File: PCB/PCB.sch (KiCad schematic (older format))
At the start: 26 parts, among them J1 , J2 , J3 PROG, SW1 ADDR, U1 ATtiny806-M

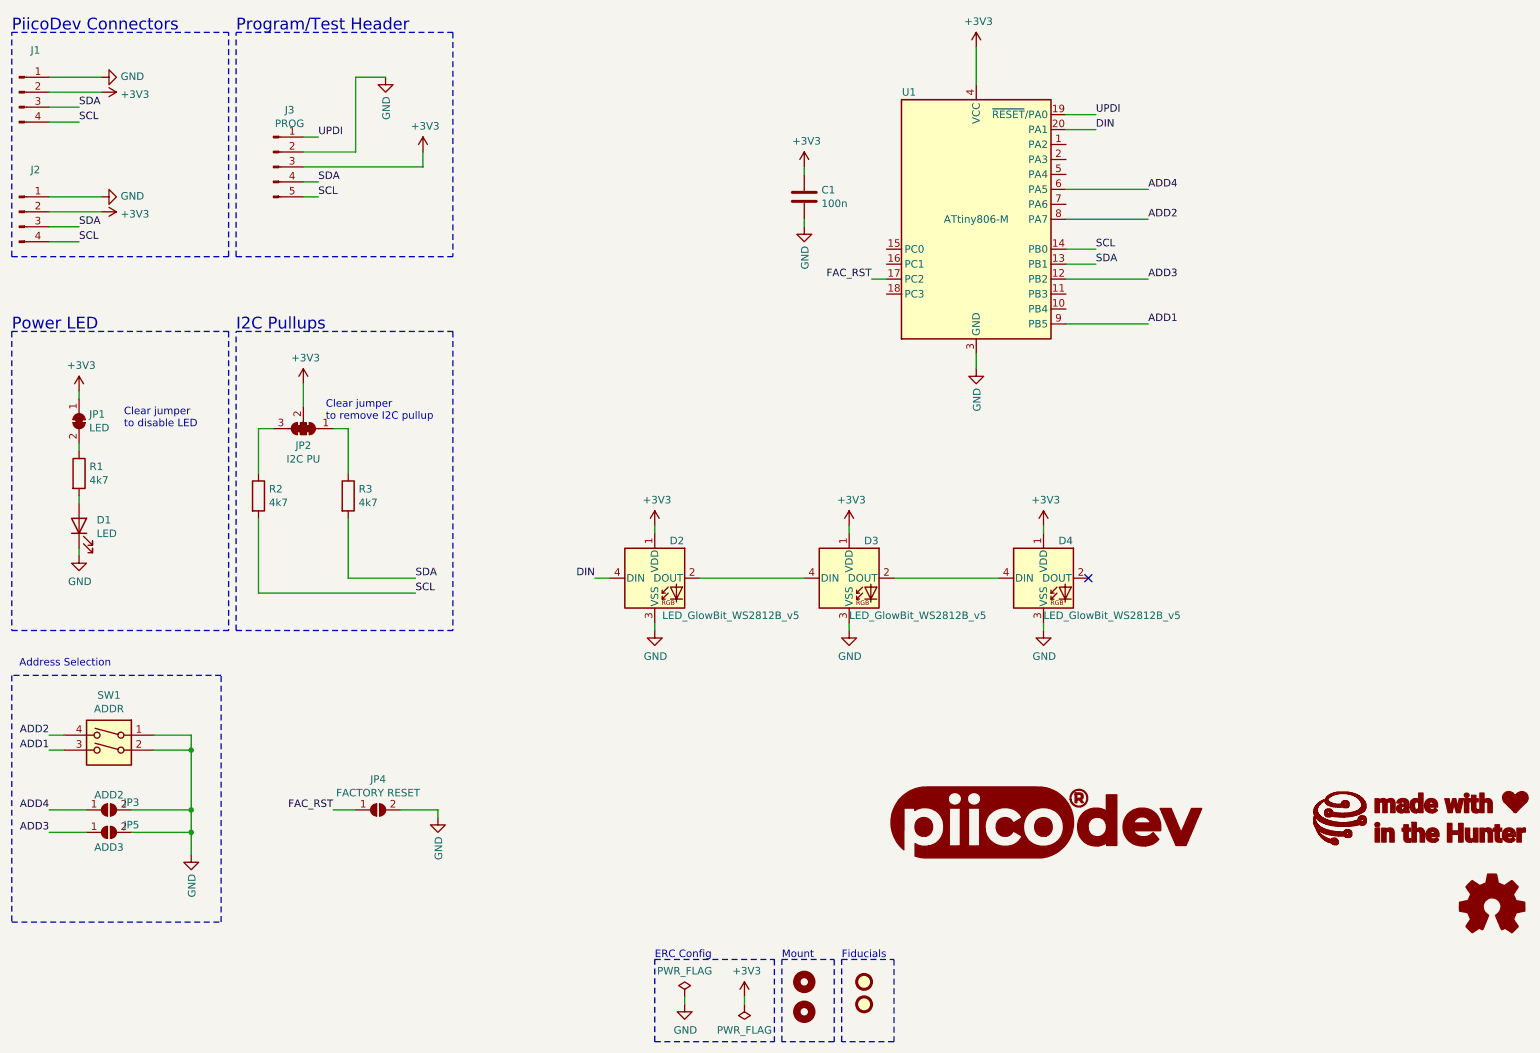
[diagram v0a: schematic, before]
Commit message: Make pwr LED user controllable
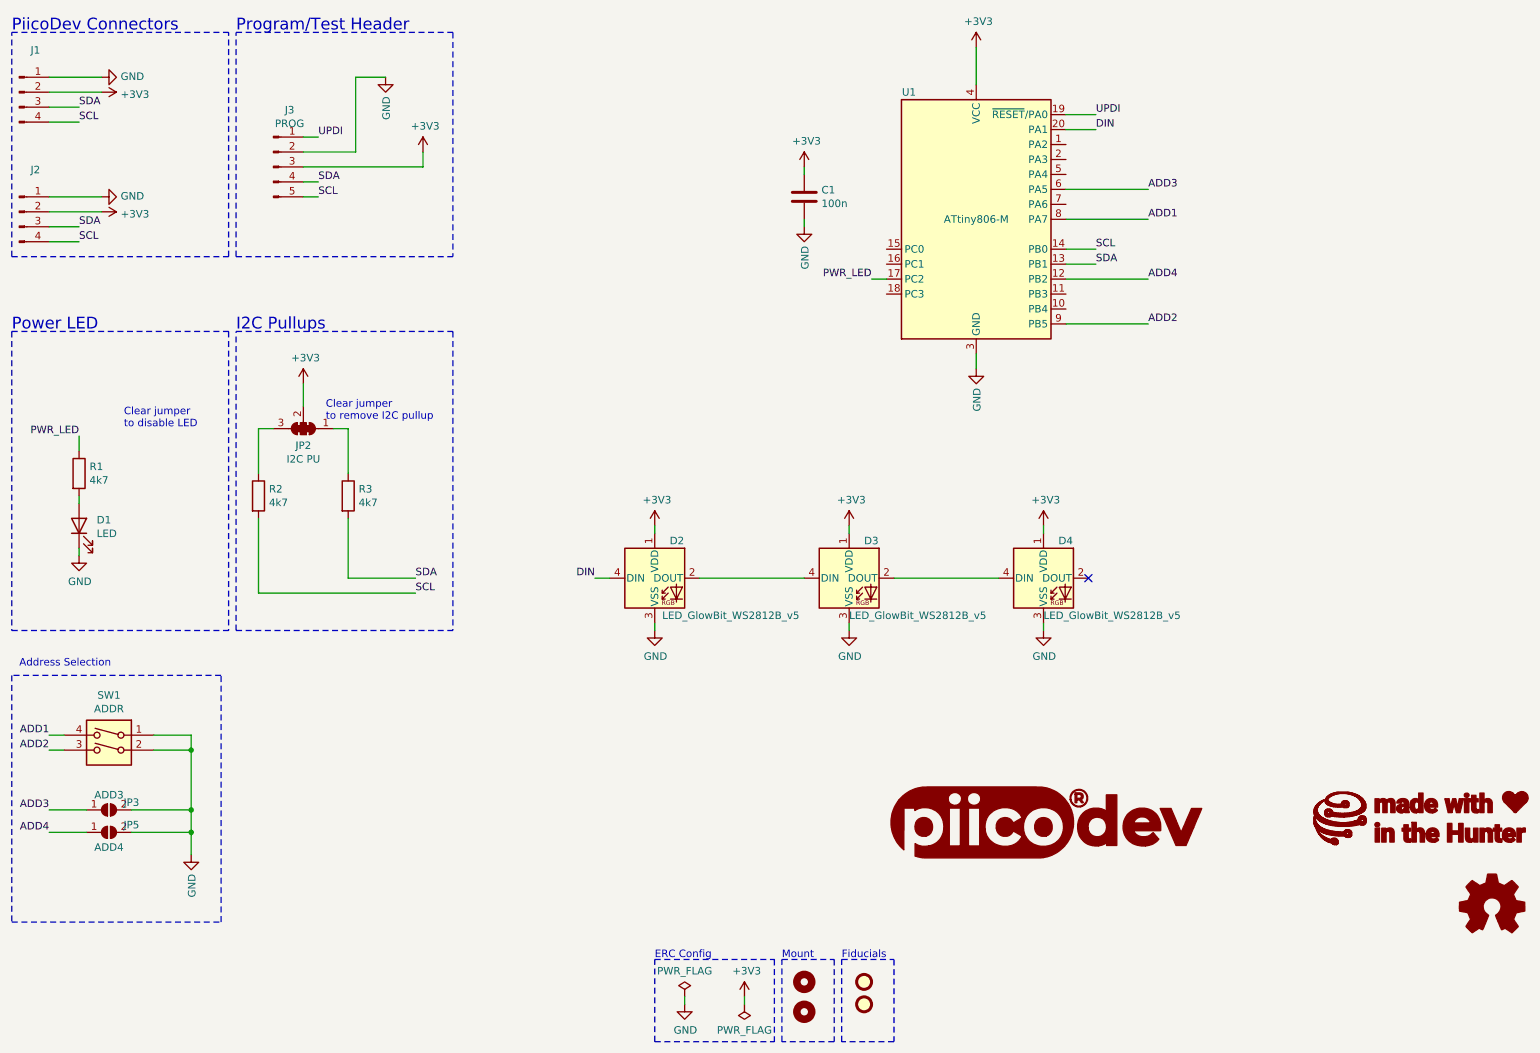
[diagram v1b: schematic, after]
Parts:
- removed JP1: LED, CoreElectronics_Components:SolderJumper-2_P1.3mm_Bridged_RoundedPad1.0x1.5mm, symbol Jumper:SolderJumper_2_Bridged
- removed JP4: FACTORY RESET, Jumper:SolderJumper-2_P1.3mm_Open_RoundedPad1.0x1.5mm, symbol Jumper:SolderJumper_2_Open
- J3: footprint CoreElectronics_Components:PiicoDev_ProgrammingHeader_2x03_P1.27mm_Vertical -> CoreElectronics_Components:PiicoDev_header_programming_test_1x05_P1.27mm_Vertical
- JP3: value ADD2 -> ADD3
- JP5: value ADD3 -> ADD4
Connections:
- net FAC_RST is gone; now on net PWR_LED: U1.17 (PC2)
- net ADD1: now also SW1.4, U1.8 (PA7); no longer SW1.3, U1.9 (PB5)
- net ADD2: now also SW1.3, U1.9 (PB5); no longer SW1.4, U1.8 (PA7)
- net ADD3: now also JP3.1 (A), U1.6 (PA5); no longer JP5.1 (A), U1.12 (PB2)
- net ADD4: now also JP5.1 (A), U1.12 (PB2); no longer JP3.1 (A), U1.6 (PA5)
- net PWR_LED: now reaches R1.1
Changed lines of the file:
@@
 Wire Wire Line
 	1450 4150 1450 4100
-Wire Wire Line
-	1450 3800 1450 3750
 $Comp
 L Device:R R1
@@
 F 3 "~" H 1450 3950 50  0001 C CNN
 	1    1450 3950
-	1    0    0    -1
-$EndComp
-Wire Wire Line
-	1450 3450 1450 3400
-$Comp
-L Jumper:SolderJumper_2_Bridged JP1
-U 1 1 60A1F615
-P 1450 3600
-F 0 "JP1" V 1404 3668 50  0000 L CNN
-F 1 "LED" V 1495 3668 50  0000 L CNN
-F 2 "CoreElectronics_Components:SolderJumper-2_P1.3mm_Bridged_RoundedPad1.0x1.5mm" H 1450 3600 50  0001 C CNN
-F 3 "~" H 1450 3600 50  0001 C CNN
-	1    1450 3600
-	0    1    1    0
-$EndComp
-$Comp
-L power:+3V3 #PWR?
-U 1 1 60A1F60F
-P 1450 3400
-F 0 "#PWR?" H 1450 3250 50  0001 C CNN
-F 1 "+3V3" H 1465 3573 50  0000 C CNN
-F 2 "" H 1450 3400 50  0001 C CNN
-F 3 "" H 1450 3400 50  0001 C CNN
-	1    1450 3400
 	1    0    0    -1
 $EndComp
@@
 F 0 "J3" H 2858 2281 50  0000 C CNN
 F 1 "PROG" H 2858 2190 50  0000 C CNN
-F 2 "CoreElectronics_Components:PiicoDev_ProgrammingHeader_2x03_P1.27mm_Vertical" H 2750 1900 50  0001 C CNN
+F 2 "CoreElectronics_Components:PiicoDev_header_programming_test_1x05_P1.27mm_Vertical" H 2750 1900 50  0001 C CNN
 F 3 "~" H 2750 1900 50  0001 C CNN
 	1    2750 1900
@@
 P 1650 6200
 F 0 "JP3" H 1800 6250 50  0000 C CNN
-F 1 "ADD2" H 1650 6300 50  0000 C CNN
+F 1 "ADD3" H 1650 6300 50  0000 C CNN
 F 2 "Jumper:SolderJumper-2_P1.3mm_Open_RoundedPad1.0x1.5mm" H 1650 6200 50  0001 C CNN
 F 3 "~" H 1650 6200 50  0001 C CNN
@@
 	2200 5700 2200 5800
 Connection ~ 2200 5800
-$Comp
-L Jumper:SolderJumper_2_Open JP4
-U 1 1 60E2F984
-P 3450 6200
-F 0 "JP4" H 3450 6405 50  0000 C CNN
-F 1 "FACTORY RESET" H 3450 6314 50  0000 C CNN
-F 2 "Jumper:SolderJumper-2_P1.3mm_Open_RoundedPad1.0x1.5mm" H 3450 6200 50  0001 C CNN
-F 3 "~" H 3450 6200 50  0001 C CNN
-	1    3450 6200
-	1    0    0    -1
-$EndComp
-$Comp
-L power:GND #PWR?
-U 1 1 60E3004B
-P 3850 6250
-AR Path="/609C5735/60E3004B" Ref="#PWR?"  Part="1"
-AR Path="/60E3004B" Ref="#PWR?"  Part="1"
-F 0 "#PWR?" H 3850 6000 50  0001 C CNN
-F 1 "GND" V 3855 6122 50  0000 R CNN
-F 2 "" H 3850 6250 50  0001 C CNN
-F 3 "" H 3850 6250 50  0001 C CNN
-	1    3850 6250
-	1    0    0    -1
-$EndComp
-Wire Wire Line
-	3850 6250 3850 6200
-Wire Wire Line
-	3850 6200 3600 6200
-Text Label 3150 6200 2    50   ~ 0
-FAC_RST
-Wire Wire Line
-	3150 6200 3300 6200
-Text Label 6750 2650 2    50   ~ 0
-FAC_RST
 Wire Wire Line
 	6750 2650 6850 2650
@@
 P 1650 6350
 F 0 "JP5" H 1800 6400 50  0000 C CNN
-F 1 "ADD3" H 1650 6250 50  0000 C CNN
+F 1 "ADD4" H 1650 6250 50  0000 C CNN
 F 2 "Jumper:SolderJumper-2_P1.3mm_Open_RoundedPad1.0x1.5mm" H 1650 6350 50  0001 C CNN
 F 3 "~" H 1650 6350 50  0001 C CNN
@@
 NoConn ~ 8200 4650
 Text Label 1250 5700 2    50   ~ 0
+ADD1
+Text Label 1250 5800 2    50   ~ 0
 ADD2
-Text Label 1250 5800 2    50   ~ 0
-ADD1
+Text Label 1250 6350 2    50   ~ 0
+ADD4
 Text Label 1250 6200 2    50   ~ 0
-ADD4
-Text Label 1250 6350 2    50   ~ 0
 ADD3
 Wire Wire Line
@@
 Address Selection
 Text Label 8600 2250 0    50   ~ 0
+ADD1
+Text Label 8600 2950 0    50   ~ 0
 ADD2
-Text Label 8600 2950 0    50   ~ 0
-ADD1
+Text Label 8600 2650 0    50   ~ 0
+ADD4
 Text Label 8600 2050 0    50   ~ 0
-ADD4
-Text Label 8600 2650 0    50   ~ 0
 ADD3
 Wire Wire Line
@@
 	-1   0    0    -1
 $EndComp
+Text Label 1450 3700 2    50   ~ 0
+PWR_LED
+Wire Wire Line
+	1450 3700 1450 3800
+Text Label 6750 2650 2    50   ~ 0
+PWR_LED
 $EndSCHEMATC

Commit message: rotate ID switch
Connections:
- net ADD1: now also SW1.2; no longer SW1.4
- net ADD2: now also SW1.1; no longer SW1.3
- net GND: now also SW1.3, SW1.4; no longer SW1.1, SW1.2
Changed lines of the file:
@@
 	2200 6350 2200 6500
 NoConn ~ 8200 4650
+Text Label 1250 5800 2    50   ~ 0
+ADD1
 Text Label 1250 5700 2    50   ~ 0
-ADD1
-Text Label 1250 5800 2    50   ~ 0
 ADD2
 Text Label 1250 6350 2    50   ~ 0
@@
 F 3 "~" H 1650 5800 50  0001 C CNN
 	1    1650 5800
-	-1   0    0    -1
+	1    0    0    -1
 $EndComp
 Text Label 1450 3700 2    50   ~ 0

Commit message: update resistors to 10k, add schematic
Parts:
- R1, R2, R3: value 4k7 -> 10k
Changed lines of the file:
@@
 Sheet 1 1
 Title "PiicoDev 3x RGB LED Module"
-Date "2021-07-09"
-Rev "v00"
+Date "2022-03-21"
+Rev "v10"
 Comp "Core Electronics"
 Comment1 ""
@@
 AR Path="/60A08162" Ref="R3"  Part="1"
 F 0 "R3" H 3320 4146 50  0000 L CNN
-F 1 "4k7" H 3320 4055 50  0000 L CNN
+F 1 "10k" H 3320 4055 50  0000 L CNN
 F 2 "Resistor_SMD:R_0402_1005Metric" V 3180 4100 50  0001 C CNN
 F 3 "~" H 3250 4100 50  0001 C CNN
@@
 AR Path="/60A08170" Ref="R2"  Part="1"
 F 0 "R2" H 2720 4146 50  0000 L CNN
-F 1 "4k7" H 2720 4055 50  0000 L CNN
+F 1 "10k" H 2720 4055 50  0000 L CNN
 F 2 "Resistor_SMD:R_0402_1005Metric" V 2580 4100 50  0001 C CNN
 F 3 "~" H 2650 4100 50  0001 C CNN
@@
 P 1450 3950
 F 0 "R1" H 1520 3996 50  0000 L CNN
-F 1 "4k7" H 1520 3905 50  0000 L CNN
+F 1 "10k" H 1520 3905 50  0000 L CNN
 F 2 "Resistor_SMD:R_0402_1005Metric" V 1380 3950 50  0001 C CNN
 F 3 "~" H 1450 3950 50  0001 C CNN
